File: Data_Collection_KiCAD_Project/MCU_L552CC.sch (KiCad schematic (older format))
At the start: 17 parts, among them U5 STM32L552CC, Y1 32MHz

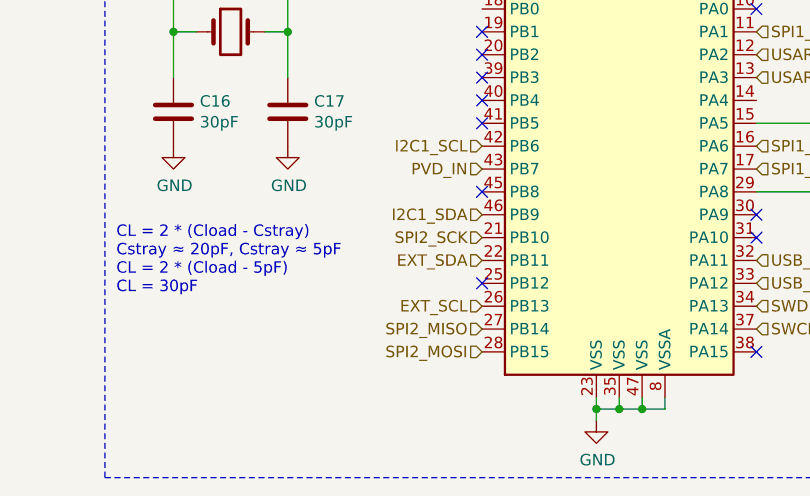
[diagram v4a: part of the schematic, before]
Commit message: Added 37Pin DSUB Main Bus
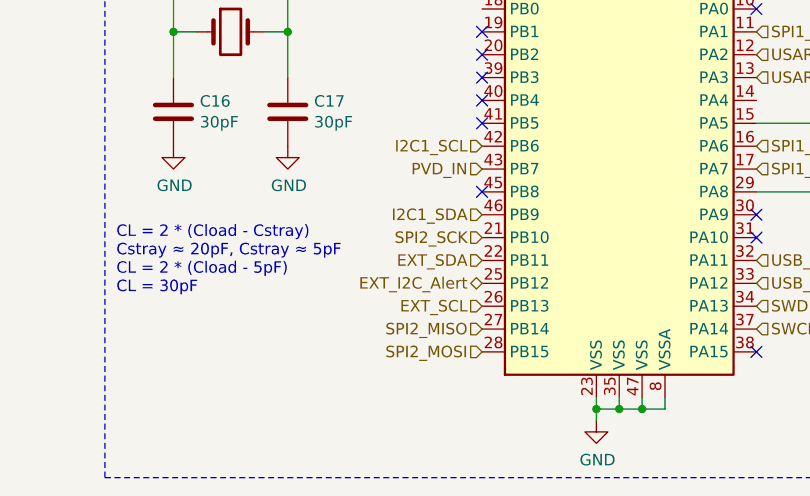
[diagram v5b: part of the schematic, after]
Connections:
- net EXT_I2C_Alert: now reaches U5.25 (PB12)
- no-connect marks 13 -> 12
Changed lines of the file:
@@
 $Descr A4 11693 8268
 encoding utf-8
-Sheet 5 9
+Sheet 5 10
 Title "STM32L552CC Schematic"
 Date "2021-10-01"
@@
 NoConn ~ 8200 4700
 NoConn ~ 8200 5000
-NoConn ~ 8200 5400
 NoConn ~ 9400 5700
 NoConn ~ 9400 5200
@@
 Text HLabel 1200 4250 2    50   Input ~ 0
 EXT_SCL
+Text HLabel 8200 5400 0    50   BiDi ~ 0
+EXT_I2C_Alert
 $EndSCHEMATC

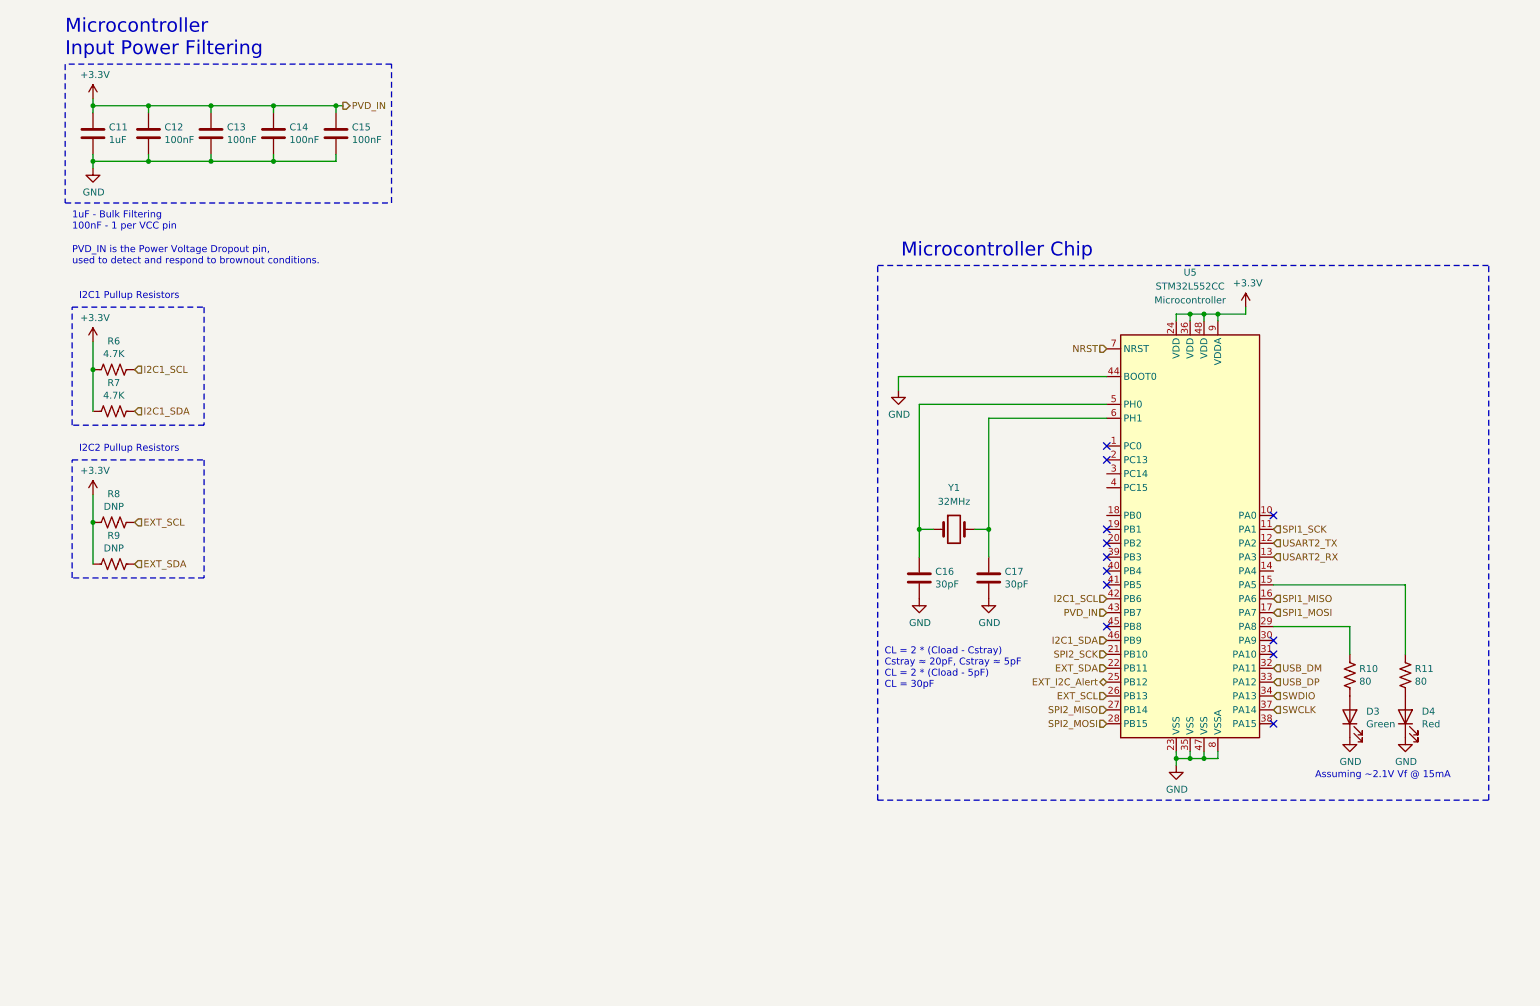
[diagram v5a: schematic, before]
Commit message: footprint changes
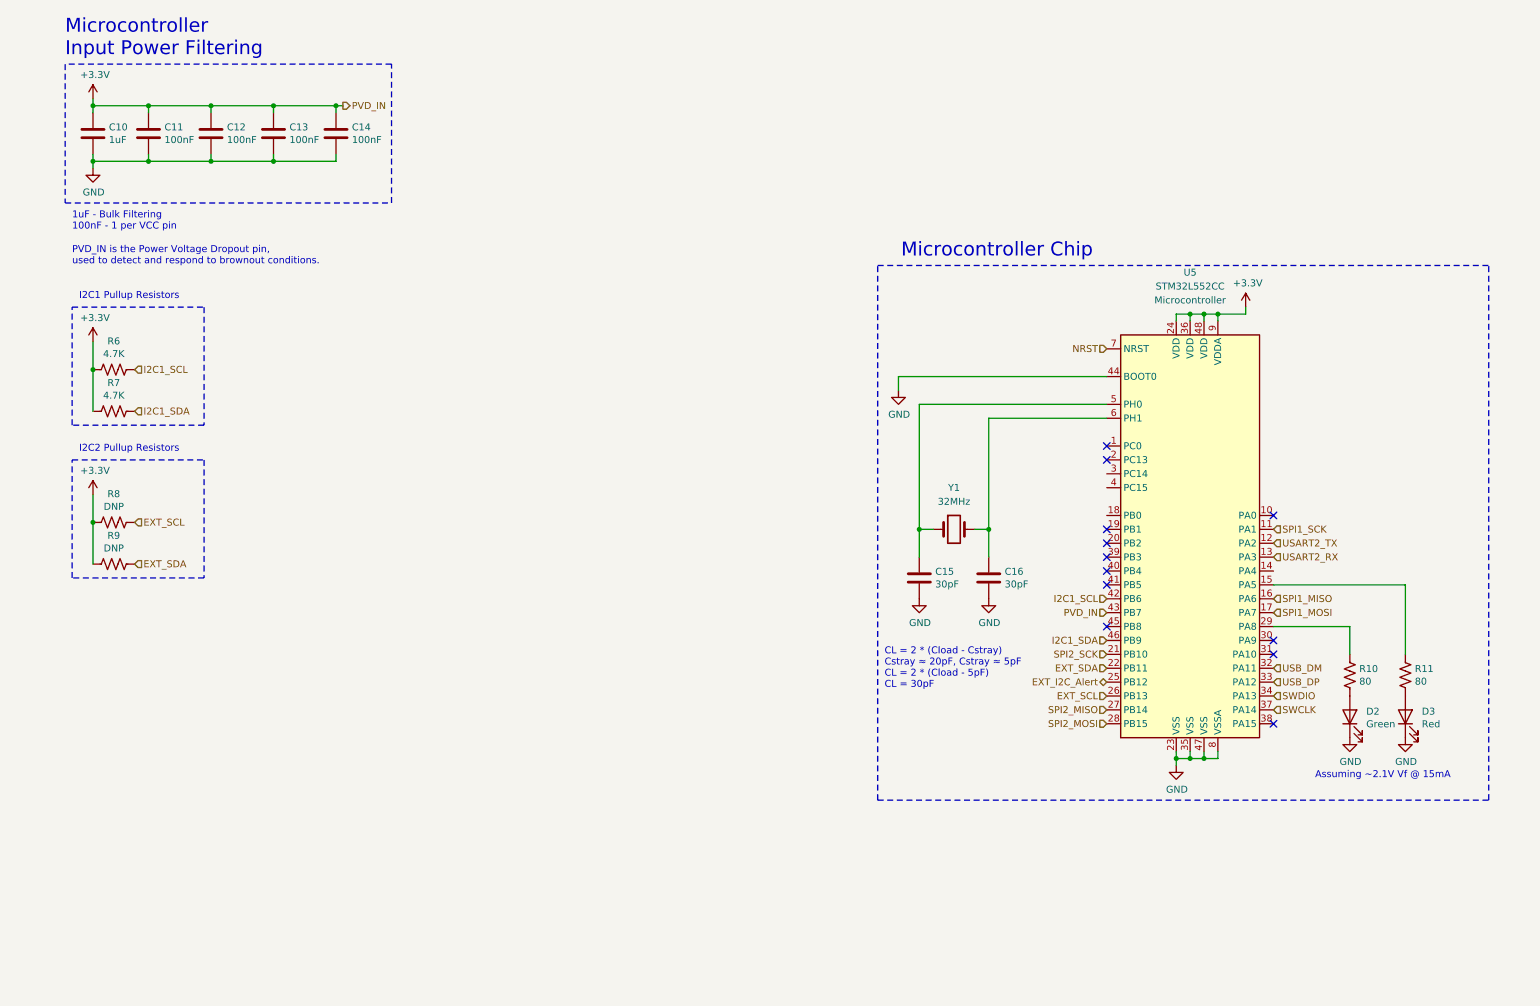
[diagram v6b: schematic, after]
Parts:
- renumbered C11 to C10, C12 to C11, C13 to C12, C14 to C13, C15 to C14, C16 to C15, C17 to C16, D3 to D2, D4 to D3
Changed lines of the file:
@@
 P 8700 6000
 AR Path="/61E9E6C6" Ref="#PWR?"  Part="1"
-AR Path="/61E8EFE4/61E9E6C6" Ref="#PWR038"  Part="1"
-F 0 "#PWR038" H 8700 5750 50  0001 C CNN
+AR Path="/61E8EFE4/61E9E6C6" Ref="#PWR031"  Part="1"
+F 0 "#PWR031" H 8700 5750 50  0001 C CNN
 F 1 "GND" H 8705 5827 50  0000 C CNN
 F 2 "" H 8700 6000 50  0001 C CNN
@@
 P 9200 2700
 AR Path="/61E9E6D6" Ref="#PWR?"  Part="1"
-AR Path="/61E8EFE4/61E9E6D6" Ref="#PWR039"  Part="1"
-F 0 "#PWR039" H 9200 2550 50  0001 C CNN
+AR Path="/61E8EFE4/61E9E6D6" Ref="#PWR032"  Part="1"
+F 0 "#PWR032" H 9200 2550 50  0001 C CNN
 F 1 "+3.3V" H 9215 2873 50  0000 C CNN
 F 2 "" H 9200 2700 50  0001 C CNN
@@
 P 6700 3300
 AR Path="/61E9E6FD" Ref="#PWR?"  Part="1"
-AR Path="/61E8EFE4/61E9E6FD" Ref="#PWR035"  Part="1"
-F 0 "#PWR035" H 6700 3050 50  0001 C CNN
+AR Path="/61E8EFE4/61E9E6FD" Ref="#PWR028"  Part="1"
+F 0 "#PWR028" H 6700 3050 50  0001 C CNN
 F 1 "GND" H 6705 3127 50  0000 C CNN
 F 2 "" H 6700 3300 50  0001 C CNN
@@
 P 9950 5650
 AR Path="/61E9E710" Ref="D?"  Part="1"
-AR Path="/61E8EFE4/61E9E710" Ref="D3"  Part="1"
-F 0 "D3" V 9989 5532 50  0000 R CNN
+AR Path="/61E8EFE4/61E9E710" Ref="D2"  Part="1"
+F 0 "D2" V 9989 5532 50  0000 R CNN
 F 1 "Green" V 9898 5532 50  0000 R CNN
 F 2 "Diode_SMD:D_0603_1608Metric_Castellated" H 9950 5650 50  0001 C CNN
@@
 P 9950 5800
 AR Path="/61E9E724" Ref="#PWR?"  Part="1"
-AR Path="/61E8EFE4/61E9E724" Ref="#PWR040"  Part="1"
-F 0 "#PWR040" H 9950 5550 50  0001 C CNN
+AR Path="/61E8EFE4/61E9E724" Ref="#PWR033"  Part="1"
+F 0 "#PWR033" H 9950 5550 50  0001 C CNN
 F 1 "GND" H 9955 5627 50  0000 C CNN
 F 2 "" H 9950 5800 50  0001 C CNN
@@
 P 6850 4650
 AR Path="/61E9E742" Ref="C?"  Part="1"
-AR Path="/61E8EFE4/61E9E742" Ref="C16"  Part="1"
-F 0 "C16" H 6965 4696 50  0000 L CNN
+AR Path="/61E8EFE4/61E9E742" Ref="C15"  Part="1"
+F 0 "C15" H 6965 4696 50  0000 L CNN
 F 1 "30pF" H 6965 4605 50  0000 L CNN
 F 2 "Capacitor_SMD:C_0603_1608Metric" H 6888 4500 50  0001 C CNN
@@
 P 7350 4650
 AR Path="/61E9E748" Ref="C?"  Part="1"
-AR Path="/61E8EFE4/61E9E748" Ref="C17"  Part="1"
-F 0 "C17" H 7465 4696 50  0000 L CNN
+AR Path="/61E8EFE4/61E9E748" Ref="C16"  Part="1"
+F 0 "C16" H 7465 4696 50  0000 L CNN
 F 1 "30pF" H 7465 4605 50  0000 L CNN
 F 2 "Capacitor_SMD:C_0603_1608Metric" H 7388 4500 50  0001 C CNN
@@
 P 6850 4800
 AR Path="/61E9E750" Ref="#PWR?"  Part="1"
-AR Path="/61E8EFE4/61E9E750" Ref="#PWR036"  Part="1"
-F 0 "#PWR036" H 6850 4550 50  0001 C CNN
+AR Path="/61E8EFE4/61E9E750" Ref="#PWR029"  Part="1"
+F 0 "#PWR029" H 6850 4550 50  0001 C CNN
 F 1 "GND" H 6855 4627 50  0000 C CNN
 F 2 "" H 6850 4800 50  0001 C CNN
@@
 P 7350 4800
 AR Path="/61E9E756" Ref="#PWR?"  Part="1"
-AR Path="/61E8EFE4/61E9E756" Ref="#PWR037"  Part="1"
-F 0 "#PWR037" H 7350 4550 50  0001 C CNN
+AR Path="/61E8EFE4/61E9E756" Ref="#PWR030"  Part="1"
+F 0 "#PWR030" H 7350 4550 50  0001 C CNN
 F 1 "GND" H 7355 4627 50  0000 C CNN
 F 2 "" H 7350 4800 50  0001 C CNN
@@
 P 900 1700
 AR Path="/61EA2645" Ref="#PWR?"  Part="1"
-AR Path="/61E8EFE4/61EA2645" Ref="#PWR032"  Part="1"
-F 0 "#PWR032" H 900 1450 50  0001 C CNN
+AR Path="/61E8EFE4/61EA2645" Ref="#PWR025"  Part="1"
+F 0 "#PWR025" H 900 1450 50  0001 C CNN
 F 1 "GND" H 905 1527 50  0000 C CNN
 F 2 "" H 900 1700 50  0001 C CNN
@@
 P 900 1450
 AR Path="/61EA264B" Ref="C?"  Part="1"
-AR Path="/61E8EFE4/61EA264B" Ref="C11"  Part="1"
-F 0 "C11" H 1015 1496 50  0000 L CNN
+AR Path="/61E8EFE4/61EA264B" Ref="C10"  Part="1"
+F 0 "C10" H 1015 1496 50  0000 L CNN
 F 1 "1uF" H 1015 1405 50  0000 L CNN
 F 2 "Capacitor_SMD:C_0603_1608Metric" H 938 1300 50  0001 C CNN
@@
 P 900 1200
 AR Path="/61EA2651" Ref="#PWR?"  Part="1"
-AR Path="/61E8EFE4/61EA2651" Ref="#PWR031"  Part="1"
-F 0 "#PWR031" H 900 1050 50  0001 C CNN
+AR Path="/61E8EFE4/61EA2651" Ref="#PWR024"  Part="1"
+F 0 "#PWR024" H 900 1050 50  0001 C CNN
 F 1 "+3.3V" H 915 1373 50  0000 C CNN
 F 2 "" H 900 1200 50  0001 C CNN
@@
 P 1300 1450
 AR Path="/61EA2659" Ref="C?"  Part="1"
-AR Path="/61E8EFE4/61EA2659" Ref="C12"  Part="1"
-F 0 "C12" H 1415 1496 50  0000 L CNN
+AR Path="/61E8EFE4/61EA2659" Ref="C11"  Part="1"
+F 0 "C11" H 1415 1496 50  0000 L CNN
 F 1 "100nF" H 1415 1405 50  0000 L CNN
 F 2 "Capacitor_SMD:C_0603_1608Metric" H 1338 1300 50  0001 C CNN
@@
 P 1750 1450
 AR Path="/61EA265F" Ref="C?"  Part="1"
-AR Path="/61E8EFE4/61EA265F" Ref="C13"  Part="1"
-F 0 "C13" H 1865 1496 50  0000 L CNN
+AR Path="/61E8EFE4/61EA265F" Ref="C12"  Part="1"
+F 0 "C12" H 1865 1496 50  0000 L CNN
 F 1 "100nF" H 1865 1405 50  0000 L CNN
 F 2 "Capacitor_SMD:C_0603_1608Metric" H 1788 1300 50  0001 C CNN
@@
 P 2200 1450
 AR Path="/61EA2665" Ref="C?"  Part="1"
-AR Path="/61E8EFE4/61EA2665" Ref="C14"  Part="1"
-F 0 "C14" H 2315 1496 50  0000 L CNN
+AR Path="/61E8EFE4/61EA2665" Ref="C13"  Part="1"
+F 0 "C13" H 2315 1496 50  0000 L CNN
 F 1 "100nF" H 2315 1405 50  0000 L CNN
 F 2 "Capacitor_SMD:C_0603_1608Metric" H 2238 1300 50  0001 C CNN
@@
 P 2650 1450
 AR Path="/61EA267F" Ref="C?"  Part="1"
-AR Path="/61E8EFE4/61EA267F" Ref="C15"  Part="1"
-F 0 "C15" H 2765 1496 50  0000 L CNN
+AR Path="/61E8EFE4/61EA267F" Ref="C14"  Part="1"
+F 0 "C14" H 2765 1496 50  0000 L CNN
 F 1 "100nF" H 2765 1405 50  0000 L CNN
 F 2 "Capacitor_SMD:C_0603_1608Metric" H 2688 1300 50  0001 C CNN
@@
 P 900 2950
 AR Path="/619E313D" Ref="#PWR?"  Part="1"
-AR Path="/61E8EFE4/619E313D" Ref="#PWR033"  Part="1"
-F 0 "#PWR033" H 900 2800 50  0001 C CNN
+AR Path="/61E8EFE4/619E313D" Ref="#PWR026"  Part="1"
+F 0 "#PWR026" H 900 2800 50  0001 C CNN
 F 1 "+3.3V" H 915 3123 50  0000 C CNN
 F 2 "" H 900 2950 50  0001 C CNN
@@
 P 10350 5650
 AR Path="/619F2F50" Ref="D?"  Part="1"
-AR Path="/61E8EFE4/619F2F50" Ref="D4"  Part="1"
-F 0 "D4" V 10389 5532 50  0000 R CNN
+AR Path="/61E8EFE4/619F2F50" Ref="D3"  Part="1"
+F 0 "D3" V 10389 5532 50  0000 R CNN
 F 1 "Red" V 10298 5532 50  0000 R CNN
 F 2 "Diode_SMD:D_0603_1608Metric_Castellated" H 10350 5650 50  0001 C CNN
@@
 P 10350 5800
 AR Path="/619F33E0" Ref="#PWR?"  Part="1"
-AR Path="/61E8EFE4/619F33E0" Ref="#PWR041"  Part="1"
-F 0 "#PWR041" H 10350 5550 50  0001 C CNN
+AR Path="/61E8EFE4/619F33E0" Ref="#PWR034"  Part="1"
+F 0 "#PWR034" H 10350 5550 50  0001 C CNN
 F 1 "GND" H 10355 5627 50  0000 C CNN
 F 2 "" H 10350 5800 50  0001 C CNN
@@
 P 900 4050
 AR Path="/61A01FA8" Ref="#PWR?"  Part="1"
-AR Path="/61E8EFE4/61A01FA8" Ref="#PWR034"  Part="1"
-F 0 "#PWR034" H 900 3900 50  0001 C CNN
+AR Path="/61E8EFE4/61A01FA8" Ref="#PWR027"  Part="1"
+F 0 "#PWR027" H 900 3900 50  0001 C CNN
 F 1 "+3.3V" H 915 4223 50  0000 C CNN
 F 2 "" H 900 4050 50  0001 C CNN

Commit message: Finalized Schematic
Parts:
- added TP10, TP11, TP12, TP13, TP5, TP6, TP7, TP8, TP9: Debug Pad, TestPoint:TestPoint_Plated_Hole_D2.0mm, symbol dk_Test-Points:RCT-0C
- Y1: footprint (none) -> Crystal:Crystal_HC49-4H_Vertical
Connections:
- net EXT_SCL: now also TP7.1
- net EXT_SDA: now also TP8.1
- net I2C1_SCL: now also TP5.1
- net I2C1_SDA: now also TP6.1
- net SPI1_MISO: now also TP12.1
- net SPI1_MOSI: now also TP13.1
- net SPI1_SCK: now also TP11.1
- net USART2_RX: now also TP10.1
- net USART2_TX: now also TP9.1
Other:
- note added: "I2C Debug Pts"
- note added: "SPI Debug"
- note added: "UART Debug"
